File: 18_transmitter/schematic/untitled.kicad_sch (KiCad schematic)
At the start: 19 parts, among them J1 RF Out, Q1 IRF510, Q2 IRF9510, Q3 FDT86256, U1 74AC04, U4 MCP1407

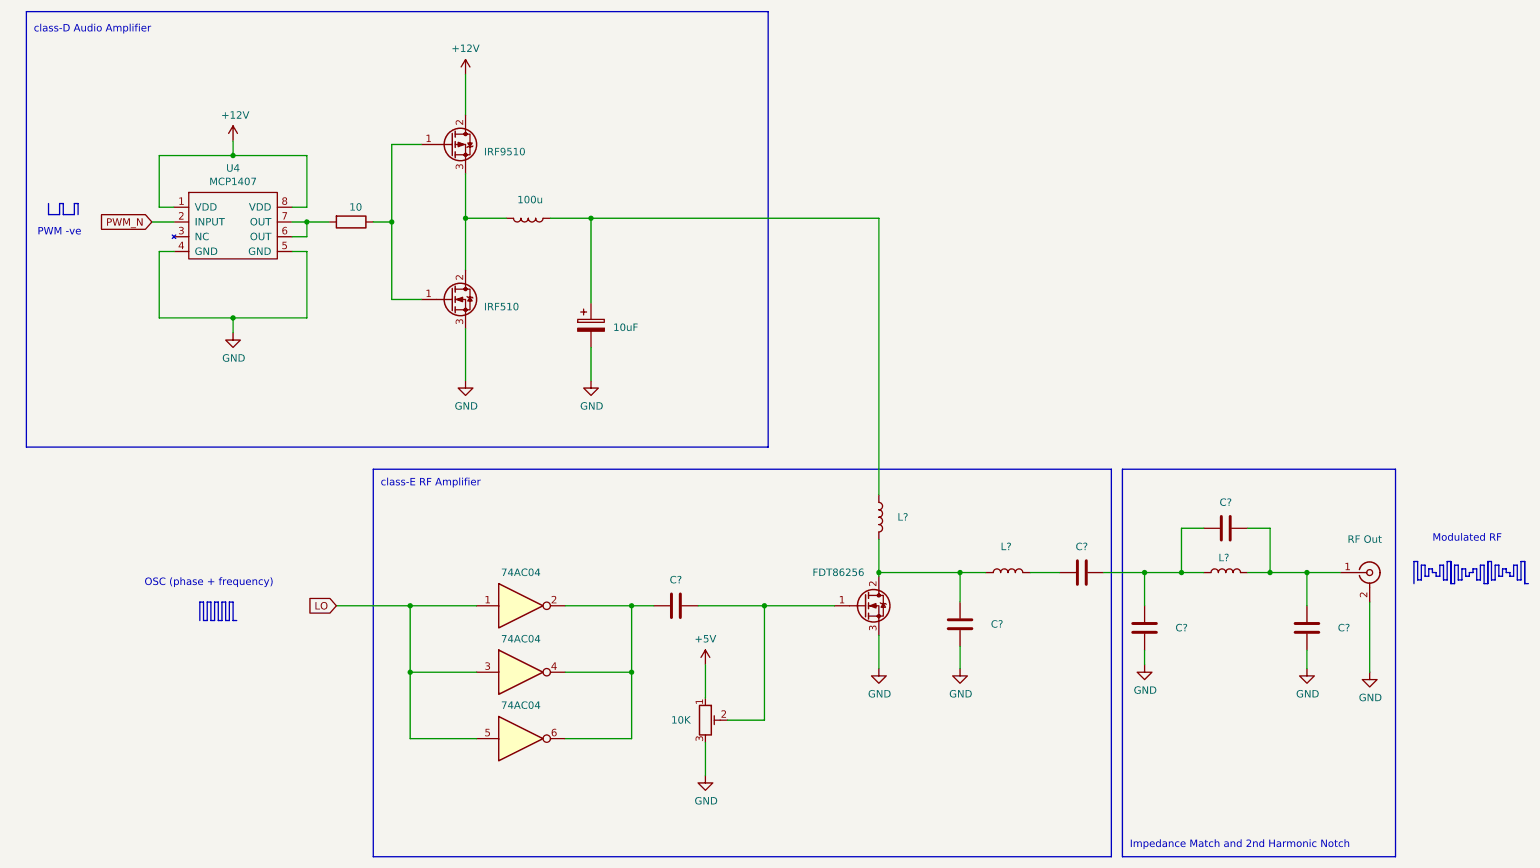
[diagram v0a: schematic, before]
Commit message: tidy up transmit python script and transmitter.cpp example
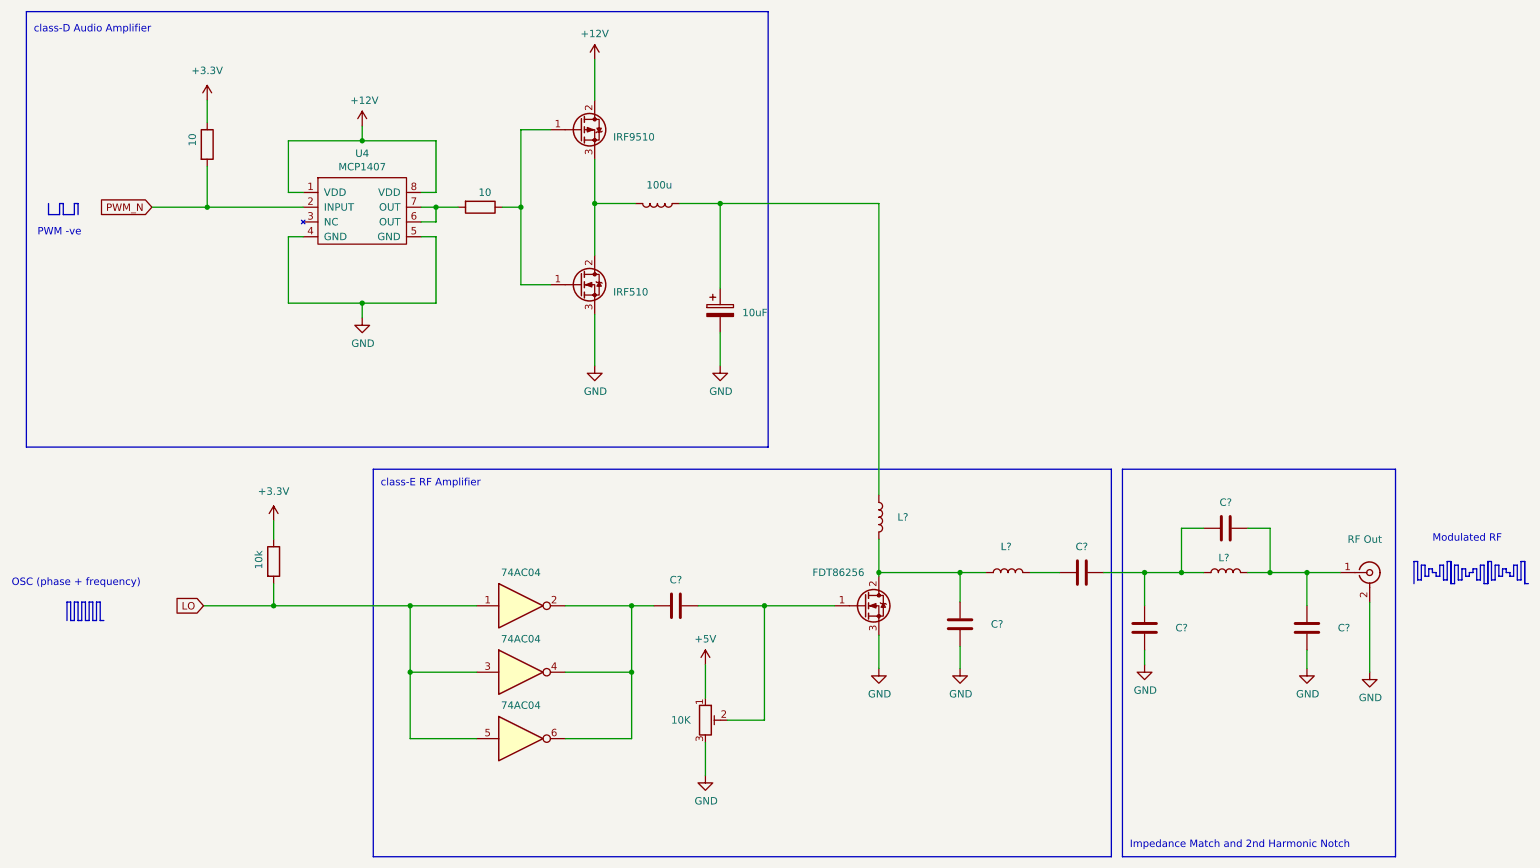
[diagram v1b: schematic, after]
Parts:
- added R?: 10, Resistor_SMD:R_0805_2012Metric, symbol Device:R
- added R?: 10k, Resistor_SMD:R_0805_2012Metric, symbol Device:R
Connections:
- net LO: now also R?.2
- net PWM_N: now also R?.2
- new net +3.3V: R?.1, R?.1
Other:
- moved on the sheet: U4
